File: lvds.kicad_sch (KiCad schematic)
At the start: 33 parts, among them J4 Conn_01x15_Female, J9 Conn_01x34_Female, U10 TPS61176RTER, U11 TCA9802, U12 NTB0102, U13 MIC5504-1.8YM5, U5 SN65DSI83TPAPRQ1

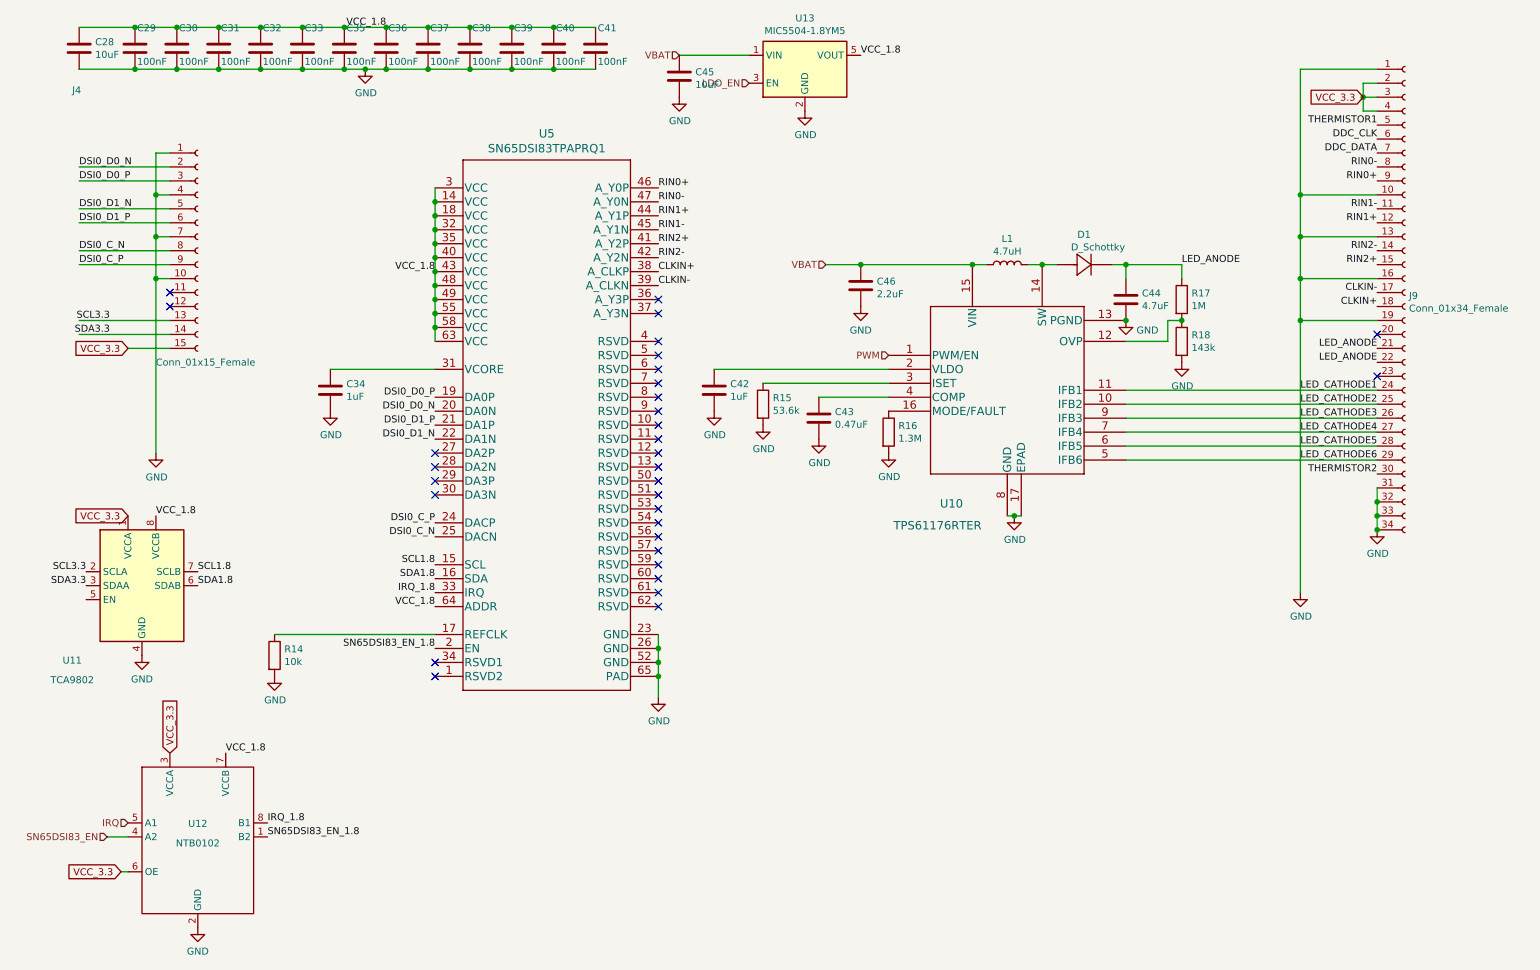
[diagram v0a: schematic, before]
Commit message: Add pinouts for dock connector; rearrange LCD backlight driver; copy the bq25895 schematic from SuperPower-RPi and add schottky to support 3.1A output on PMID.
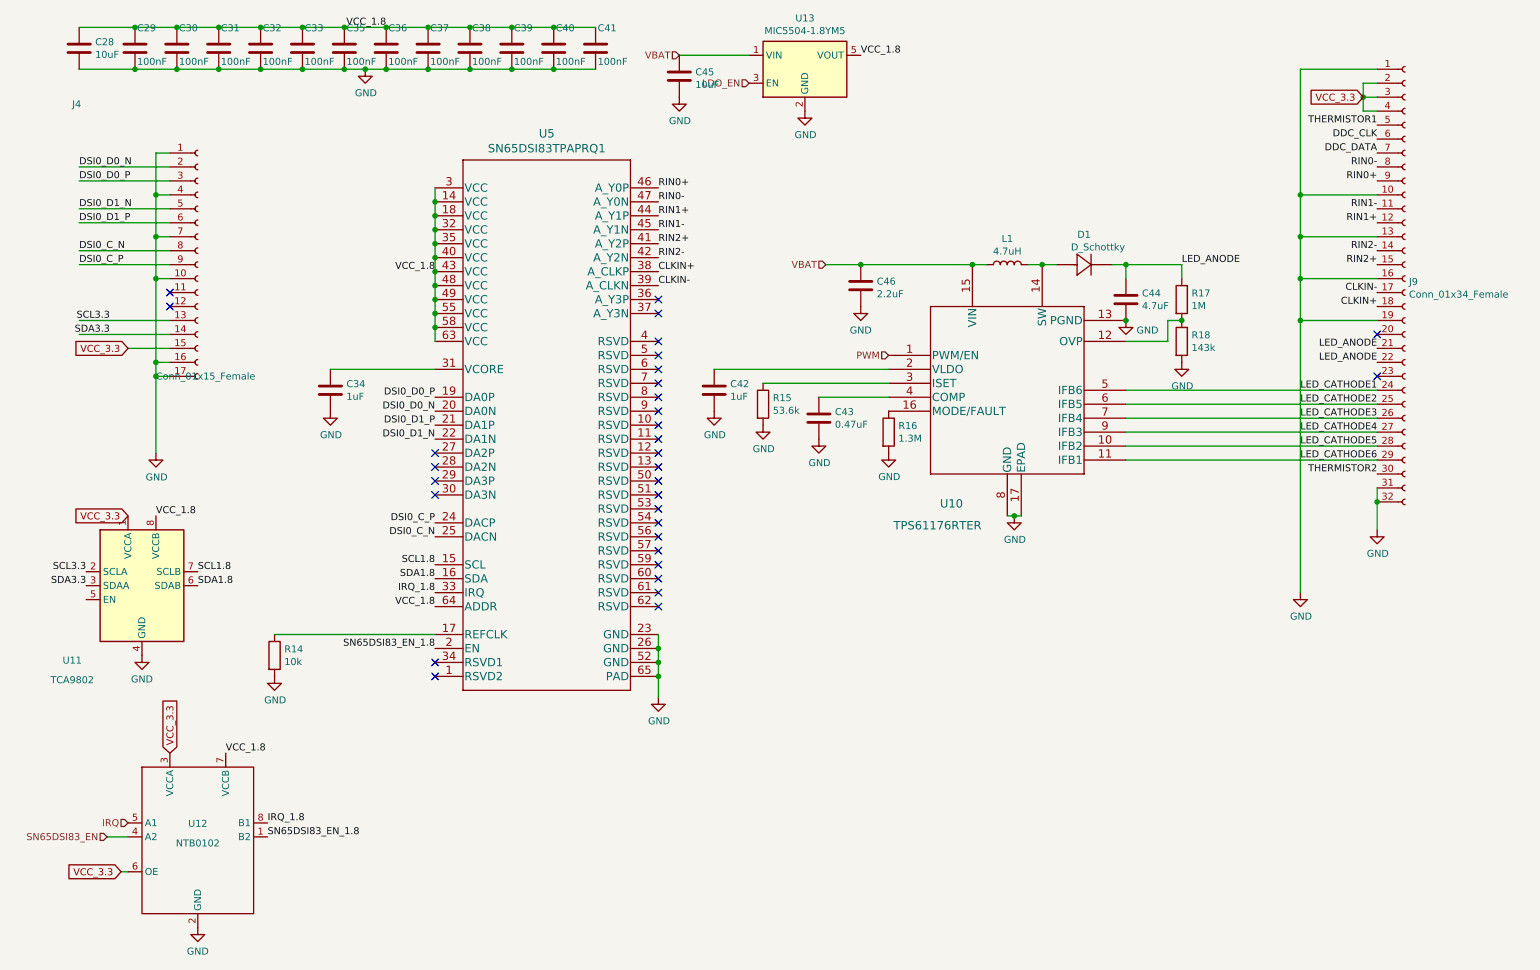
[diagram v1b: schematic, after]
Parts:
- C44: footprint Capacitor_SMD:C_0402_1005Metric -> Capacitor_SMD:C_0603_1608Metric
- J4: symbol Connector:Conn_01x15_Female -> Connector:Conn_01x17_Female
- J9: symbol Connector:Conn_01x34_Female -> Connector:Conn_01x32_Female
- L1: footprint Inductor_SMD:L_0603_1608Metric_Pad1.05x0.95mm_HandSolder -> Inductor_SMD:L_0805_2012Metric; Digi-Key PN (none) -> MLZ2012N4R7LT000
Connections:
- net GND: now also J4.16 (Pin_16), J4.17 (Pin_17); no longer J9.33 (Pin_33), J9.34 (Pin_34)
- net LED_CATHODE1: now also U10.5 (IFB6); no longer U10.11 (IFB1)
- net LED_CATHODE2: now also U10.6 (IFB5); no longer U10.10 (IFB2)
- net LED_CATHODE3: now also U10.7 (IFB4); no longer U10.9 (IFB3)
- net LED_CATHODE4: now also U10.9 (IFB3); no longer U10.7 (IFB4)
- net LED_CATHODE5: now also U10.10 (IFB2); no longer U10.6 (IFB5)
- net LED_CATHODE6: now also U10.11 (IFB1); no longer U10.5 (IFB6)
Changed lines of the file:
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@@
   (junction (at 39.37 59.69) (diameter 1.016) (color 0 0 0 0))
   (junction (at 39.37 67.31) (diameter 1.016) (color 0 0 0 0))
+  (junction (at 39.37 82.55) (diameter 1.016) (color 0 0 0 0))
+  (junction (at 39.37 85.09) (diameter 1.016) (color 0 0 0 0))
   (junction (at 43.18 21.59) (diameter 1.016) (color 0 0 0 0))
   (junction (at 43.18 29.21) (diameter 1.016) (color 0 0 0 0))
@@
   (junction (at 259.08 34.29) (diameter 1.016) (color 0 0 0 0))
   (junction (at 261.62 107.95) (diameter 1.016) (color 0 0 0 0))
-  (junction (at 261.62 110.49) (diameter 1.016) (color 0 0 0 0))
-  (junction (at 261.62 113.03) (diameter 1.016) (color 0 0 0 0))
   (no_connect (at 41.91 69.85))
   (no_connect (at 41.91 72.39))
@@
     (stroke (width 0) (type solid) (color 0 0 0 0))
   )
-  (wire (pts (xy 39.37 67.31) (xy 39.37 99.06))
+  (wire (pts (xy 39.37 67.31) (xy 39.37 82.55))
     (stroke (width 0) (type solid) (color 0 0 0 0))
   )
@@
     (stroke (width 0) (type solid) (color 0 0 0 0))
   )
+  (wire (pts (xy 39.37 82.55) (xy 39.37 85.09))
+    (stroke (width 0) (type solid) (color 0 0 0 0))
+  )
+  (wire (pts (xy 39.37 82.55) (xy 41.91 82.55))
+    (stroke (width 0) (type solid) (color 0 0 0 0))
+  )
+  (wire (pts (xy 39.37 85.09) (xy 39.37 99.06))
+    (stroke (width 0) (type solid) (color 0 0 0 0))
+  )
+  (wire (pts (xy 39.37 85.09) (xy 41.91 85.09))
+    (stroke (width 0) (type solid) (color 0 0 0 0))
+  )
   (wire (pts (xy 41.91 44.45) (xy 39.37 44.45))
     (stroke (width 0) (type solid) (color 0 0 0 0))
@@
     (stroke (width 0) (type solid) (color 0 0 0 0))
   )
-  (wire (pts (xy 261.62 107.95) (xy 261.62 110.49))
-    (stroke (width 0) (type solid) (color 0 0 0 0))
-  )
-  (wire (pts (xy 261.62 110.49) (xy 261.62 113.03))
+  (wire (pts (xy 261.62 107.95) (xy 261.62 113.03))
     (stroke (width 0) (type solid) (color 0 0 0 0))
   )
@@
     (property "Reference" "L1" (id 0) (at 194.31 60.0518 90))
     (property "Value" "4.7uH" (id 1) (at 194.31 62.35 90))
-    (property "Footprint" "Inductor_SMD:L_0603_1608Metric_Pad1.05x0.95mm_HandSolder" (id 2) (at 194.31 64.77 0)
+    (property "Footprint" "Inductor_SMD:L_0805_2012Metric" (id 2) (at 194.31 64.77 0)
       (effects (font (size 1.27 1.27)) hide)
     )
     (property "Datasheet" "~" (id 3) (at 194.31 64.77 0)
+      (effects (font (size 1.27 1.27)) hide)
+    )
+    (property "Digi-Key PN" "MLZ2012N4R7LT000" (id 4) (at 194.31 64.77 0)
       (effects (font (size 1.27 1.27)) hide)
     )
@@
       (effects (font (size 1.27 1.27)) (justify left))
     )
-    (property "Footprint" "Capacitor_SMD:C_0402_1005Metric" (id 2) (at 216.8652 74.93 0)
+    (property "Footprint" "Capacitor_SMD:C_0603_1608Metric" (id 2) (at 216.8652 74.93 0)
       (effects (font (size 1.27 1.27)) hide)
     )
@@
     (pin "2")
   )
-  (symbol (lib_id "Connector:Conn_01x15_Female") (at 46.99 62.23 0) (unit 1)
-    (in_bom yes) (on_board yes)
-    (property "Reference" "J4" (id 0) (at 24.13 33.02 0)
-      (effects (font (size 1.27 1.27)) (justify left))
-    )
-    (property "Value" "Conn_01x15_Female" (id 1) (at 39.37 82.55 0)
-      (effects (font (size 1.27 1.27)) (justify left))
-    )
-    (property "Footprint" "footprints:SFW15R-2STE1LF" (id 2) (at 46.99 62.23 0)
-      (effects (font (size 1.27 1.27)) hide)
-    )
-    (property "Datasheet" "~" (id 3) (at 46.99 62.23 0)
-      (effects (font (size 1.27 1.27)) hide)
-    )
-    (property "Field4" "Mouser" (id 4) (at 46.99 62.23 0)
-      (effects (font (size 1.27 1.27)) hide)
-    )
-    (property "Field5" "798-FH12-22S-0.5SH55" (id 5) (at 46.99 62.23 0)
-      (effects (font (size 1.27 1.27)) hide)
-    )
-    (property "Field6" "FH12-22S-0.5SH55" (id 6) (at 46.99 62.23 0)
-      (effects (font (size 1.27 1.27)) hide)
-    )
-    (property "Field7" "Hirose" (id 7) (at 46.99 62.23 0)
-      (effects (font (size 1.27 1.27)) hide)
-    )
-    (property "Part Description" "22 Position FFC, FPC Connector Contacts, Bottom 0.020\" (0.50mm) Surface Mount, Right Angle" (id 8) (at 46.99 62.23 0)
+  (symbol (lib_id "Connector:Conn_01x17_Female") (at 46.99 64.77 0) (unit 1)
+    (in_bom yes) (on_board yes)
+    (property "Reference" "J4" (id 0) (at 24.13 35.56 0)
+      (effects (font (size 1.27 1.27)) (justify left))
+    )
+    (property "Value" "Conn_01x15_Female" (id 1) (at 39.37 85.09 0)
+      (effects (font (size 1.27 1.27)) (justify left))
+    )
+    (property "Footprint" "footprints:SFW15R-2STE1LF" (id 2) (at 46.99 64.77 0)
+      (effects (font (size 1.27 1.27)) hide)
+    )
+    (property "Datasheet" "~" (id 3) (at 46.99 64.77 0)
+      (effects (font (size 1.27 1.27)) hide)
+    )
+    (property "Field4" "Mouser" (id 4) (at 46.99 64.77 0)
+      (effects (font (size 1.27 1.27)) hide)
+    )
+    (property "Field5" "798-FH12-22S-0.5SH55" (id 5) (at 46.99 64.77 0)
+      (effects (font (size 1.27 1.27)) hide)
+    )
+    (property "Field6" "FH12-22S-0.5SH55" (id 6) (at 46.99 64.77 0)
+      (effects (font (size 1.27 1.27)) hide)
+    )
+    (property "Field7" "Hirose" (id 7) (at 46.99 64.77 0)
+      (effects (font (size 1.27 1.27)) hide)
+    )
+    (property "Part Description" "22 Position FFC, FPC Connector Contacts, Bottom 0.020\" (0.50mm) Surface Mount, Right Angle" (id 8) (at 46.99 64.77 0)
       (effects (font (size 1.27 1.27)) hide)
     )
@@
     (pin "14")
     (pin "15")
+    (pin "16")
+    (pin "17")
     (pin "2")
     (pin "3")
@@
     (pin "5")
   )
-  (symbol (lib_id "Connector:Conn_01x34_Female") (at 266.7 69.85 0) (unit 1)
-    (in_bom yes) (on_board yes)
-    (property "Reference" "J9" (id 0) (at 267.411 70.428 0)
-      (effects (font (size 1.27 1.27)) (justify left))
-    )
-    (property "Value" "Conn_01x34_Female" (id 1) (at 267.4113 72.7265 0)
-      (effects (font (size 1.27 1.27)) (justify left))
-    )
-    (property "Footprint" "footprints:20474-030E-11" (id 2) (at 266.7 69.85 0)
-      (effects (font (size 1.27 1.27)) hide)
-    )
-    (property "Datasheet" "~" (id 3) (at 266.7 69.85 0)
+  (symbol (lib_id "Connector:Conn_01x32_Female") (at 266.7 67.31 0) (unit 1)
+    (in_bom yes) (on_board yes)
+    (property "Reference" "J9" (id 0) (at 267.411 67.888 0)
+      (effects (font (size 1.27 1.27)) (justify left))
+    )
+    (property "Value" "Conn_01x34_Female" (id 1) (at 267.4113 70.1865 0)
+      (effects (font (size 1.27 1.27)) (justify left))
+    )
+    (property "Footprint" "footprints:20474-030E-11" (id 2) (at 266.7 67.31 0)
+      (effects (font (size 1.27 1.27)) hide)
+    )
+    (property "Datasheet" "~" (id 3) (at 266.7 67.31 0)
       (effects (font (size 1.27 1.27)) hide)
     )
@@
     (pin "31")
     (pin "32")
-    (pin "33")
-    (pin "34")
     (pin "4")
     (pin "5")

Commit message: Switch some footprints to minimize BOM costs. Cache a bunch more datasheets and documentation
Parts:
- R14, R15, R16, R17, R18: footprint Resistor_SMD:R_0402_1005Metric_Pad0.72x0.64mm_HandSolder -> Resistor_SMD:R_0402_1005Metric
- U12: footprint Package_SO:TSSOP-8_3x3mm_P0.65mm -> footprints:SOT833-1
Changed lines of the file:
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@@
       (effects (font (size 1.27 1.27)) (justify left))
     )
-    (property "Footprint" "Resistor_SMD:R_0402_1005Metric_Pad0.72x0.64mm_HandSolder" (id 2) (at 59.182 135.89 90)
+    (property "Footprint" "Resistor_SMD:R_0402_1005Metric" (id 2) (at 59.182 135.89 90)
       (effects (font (size 1.27 1.27)) hide)
     )
@@
       (effects (font (size 1.27 1.27)) (justify left))
     )
-    (property "Footprint" "Resistor_SMD:R_0402_1005Metric_Pad0.72x0.64mm_HandSolder" (id 2) (at 148.082 90.17 90)
+    (property "Footprint" "Resistor_SMD:R_0402_1005Metric" (id 2) (at 148.082 90.17 90)
       (effects (font (size 1.27 1.27)) hide)
     )
@@
       (effects (font (size 1.27 1.27)) (justify left))
     )
-    (property "Footprint" "Resistor_SMD:R_0402_1005Metric_Pad0.72x0.64mm_HandSolder" (id 2) (at 170.942 95.25 90)
+    (property "Footprint" "Resistor_SMD:R_0402_1005Metric" (id 2) (at 170.942 95.25 90)
       (effects (font (size 1.27 1.27)) hide)
     )
@@
       (effects (font (size 1.27 1.27)) (justify left))
     )
-    (property "Footprint" "Resistor_SMD:R_0402_1005Metric_Pad0.72x0.64mm_HandSolder" (id 2) (at 224.282 71.12 90)
+    (property "Footprint" "Resistor_SMD:R_0402_1005Metric" (id 2) (at 224.282 71.12 90)
       (effects (font (size 1.27 1.27)) hide)
     )
@@
       (effects (font (size 1.27 1.27)) (justify left))
     )
-    (property "Footprint" "Resistor_SMD:R_0402_1005Metric_Pad0.72x0.64mm_HandSolder" (id 2) (at 224.282 78.74 90)
+    (property "Footprint" "Resistor_SMD:R_0402_1005Metric" (id 2) (at 224.282 78.74 90)
       (effects (font (size 1.27 1.27)) hide)
     )
@@
     (property "Reference" "U12" (id 0) (at 46.99 166.4928 0))
     (property "Value" "NTB0102" (id 1) (at 46.99 170.0615 0))
-    (property "Footprint" "Package_SO:TSSOP-8_3x3mm_P0.65mm" (id 2) (at 46.99 167.64 0)
-      (effects (font (size 1.27 1.27)) hide)
-    )
+    (property "Footprint" "footprints:SOT833-1" (id 2) (at 46.99 167.64 0)
+      (effects (font (size 1.27 1.27)) hide)
+    )
